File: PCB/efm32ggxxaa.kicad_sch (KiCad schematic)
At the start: 8 parts, among them U5 EFM32GG11B420F2048GQ100

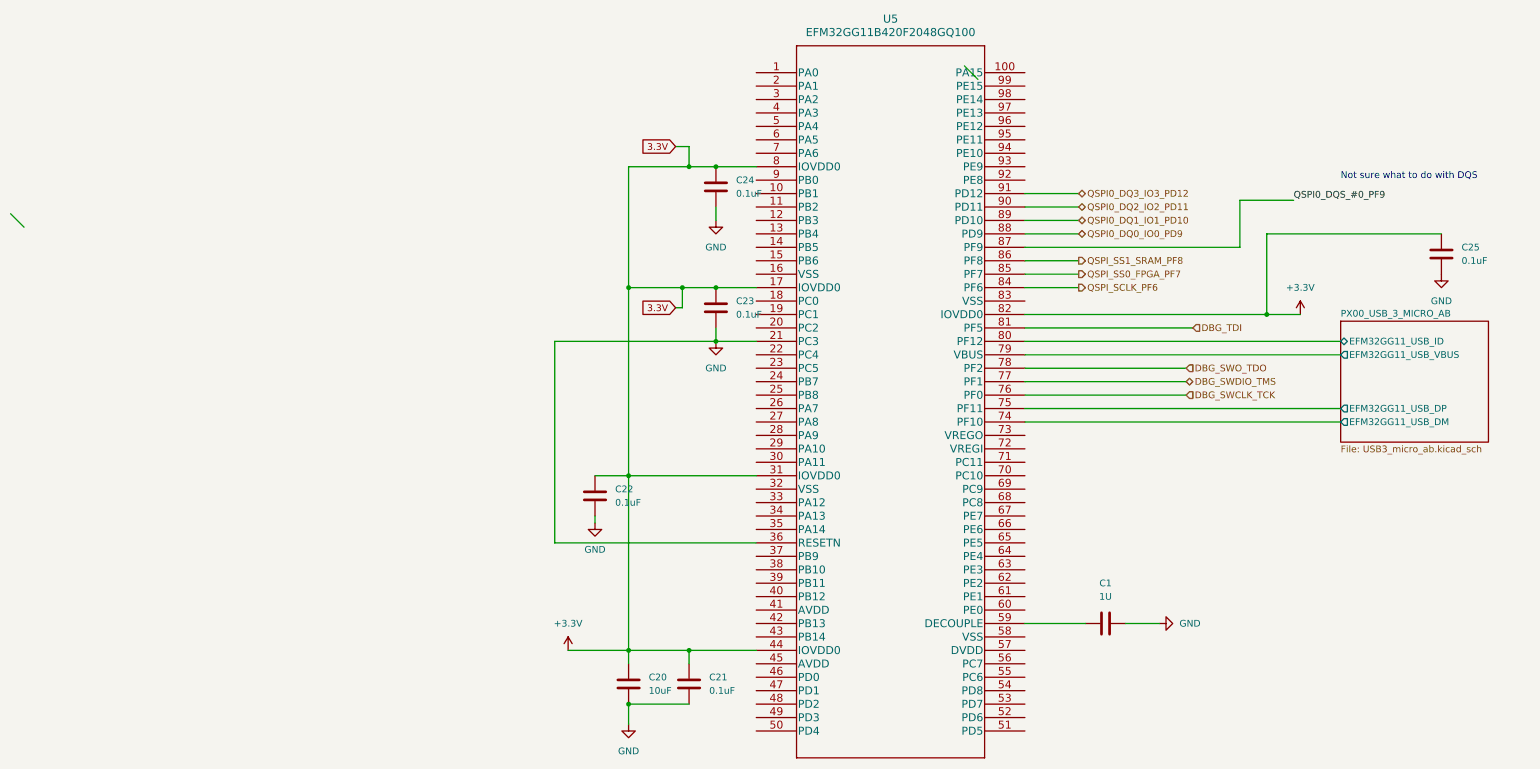
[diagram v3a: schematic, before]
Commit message: Attempt to set up SRAM
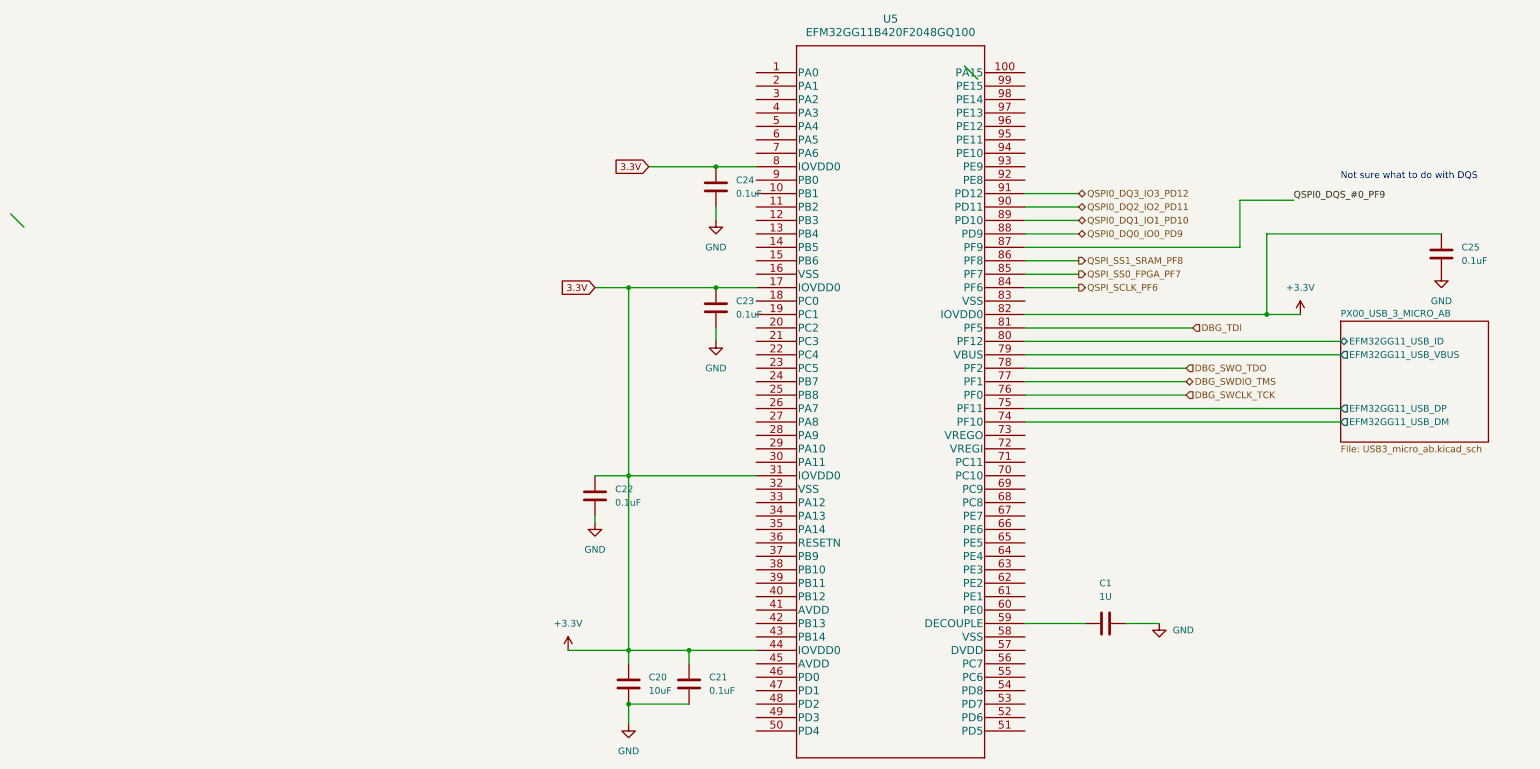
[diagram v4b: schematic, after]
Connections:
- net GND: no longer U5.21 (PC3), U5.36 (RESETN)
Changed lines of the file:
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@@
   (junction (at 99.06 107.95) (diameter 0) (color 0 0 0 0)
   )
-  (junction (at 109.22 72.39) (diameter 0) (color 0 0 0 0)
-  )
   (junction (at 115.57 49.53) (diameter 0) (color 0 0 0 0)
   )
@@
   (junction (at 99.06 140.97) (diameter 0) (color 0 0 0 0)
   )
-  (junction (at 110.49 49.53) (diameter 0) (color 0 0 0 0)
-  )
   (junction (at 219.71 77.47) (diameter 0) (color 0 0 0 0)
   )
-  (junction (at 115.57 82.55) (diameter 0) (color 0 0 0 0)
-  )
   (junction (at 115.57 72.39) (diameter 0) (color 0 0 0 0)
   )
@@
     (stroke (width 0) (type default))
   )
-  (wire (pts (xy 85.09 120.65) (xy 123.19 120.65))
-    (stroke (width 0) (type default))
-  )
   (wire (pts (xy 87.63 140.97) (xy 99.06 140.97))
     (stroke (width 0) (type default))
@@
     (stroke (width 0) (type default))
   )
-  (wire (pts (xy 99.06 49.53) (xy 99.06 72.39))
-    (stroke (width 0) (type default))
-  )
-  (wire (pts (xy 107.95 45.72) (xy 110.49 45.72))
-    (stroke (width 0) (type default))
-  )
   (wire (pts (xy 173.99 92.71) (xy 204.47 92.71))
     (stroke (width 0) (type default))
   )
-  (wire (pts (xy 110.49 49.53) (xy 115.57 49.53))
+  (wire (pts (xy 102.87 49.53) (xy 115.57 49.53))
     (stroke (width 0) (type default))
   )
@@
     (stroke (width 0) (type default))
   )
-  (wire (pts (xy 109.22 72.39) (xy 115.57 72.39))
-    (stroke (width 0) (type default))
-  )
   (wire (pts (xy 219.71 62.23) (xy 252.73 62.23))
     (stroke (width 0) (type default))
   )
-  (wire (pts (xy 115.57 82.55) (xy 123.19 82.55))
-    (stroke (width 0) (type default))
-  )
   (wire (pts (xy 99.06 140.97) (xy 110.49 140.97))
     (stroke (width 0) (type default))
@@
     (stroke (width 0) (type default))
   )
-  (wire (pts (xy 109.22 76.2) (xy 109.22 72.39))
-    (stroke (width 0) (type default))
-  )
-  (wire (pts (xy 85.09 82.55) (xy 85.09 120.65))
-    (stroke (width 0) (type default))
-  )
   (wire (pts (xy 115.57 49.53) (xy 123.19 49.53))
     (stroke (width 0) (type default))
@@
     (stroke (width 0) (type default))
   )
-  (wire (pts (xy 107.95 76.2) (xy 109.22 76.2))
+  (wire (pts (xy 92.71 72.39) (xy 99.06 72.39))
     (stroke (width 0) (type default))
   )
@@
     (stroke (width 0) (type default))
   )
-  (wire (pts (xy 99.06 49.53) (xy 110.49 49.53))
-    (stroke (width 0) (type default))
-  )
   (wire (pts (xy 173.99 87.63) (xy 204.47 87.63))
     (stroke (width 0) (type default))
@@
     (stroke (width 0) (type default))
   )
-  (wire (pts (xy 99.06 72.39) (xy 109.22 72.39))
+  (wire (pts (xy 99.06 72.39) (xy 115.57 72.39))
     (stroke (width 0) (type default))
   )
@@
     (stroke (width 0) (type default))
   )
-  (wire (pts (xy 110.49 45.72) (xy 110.49 49.53))
-    (stroke (width 0) (type default))
-  )
   (wire (pts (xy 173.99 62.23) (xy 184.15 62.23))
     (stroke (width 0) (type default))
@@
   )
   (wire (pts (xy 173.99 59.69) (xy 184.15 59.69))
-    (stroke (width 0) (type default))
-  )
-  (wire (pts (xy 85.09 82.55) (xy 115.57 82.55))
     (stroke (width 0) (type default))
   )
@@
     (effects (font (size 1.27 1.27)) (justify left bottom))
   )
-  (global_label "3.3V" (shape input) (at 107.95 45.72 180) (fields_autoplaced)
+  (global_label "3.3V" (shape input) (at 102.87 49.53 180) (fields_autoplaced)
     (effects (font (size 1.27 1.27)) (justify right))
-    (property "Intersheetrefs" "${INTERSHEET_REFS}" (at 100.8524 45.72 0)
+    (property "Intersheetrefs" "${INTERSHEET_REFS}" (at 95.7724 49.53 0)
       (effects (font (size 1.27 1.27)) (justify right) hide)
     )
   )
-  (global_label "3.3V" (shape input) (at 107.95 76.2 180) (fields_autoplaced)
+  (global_label "3.3V" (shape input) (at 92.71 72.39 180) (fields_autoplaced)
     (effects (font (size 1.27 1.27)) (justify right))
-    (property "Intersheetrefs" "${INTERSHEET_REFS}" (at 100.8524 76.2 0)
+    (property "Intersheetrefs" "${INTERSHEET_REFS}" (at 85.6124 72.39 0)
       (effects (font (size 1.27 1.27)) (justify right) hide)
     )
@@
     )
   )
-  (symbol (lib_id "power:GND") (at 199.39 135.89 90) (unit 1)
-    (in_bom yes) (on_board yes) (dnp no) (fields_autoplaced)
-    (property "Reference" "#PWR07" (at 205.74 135.89 0)
-      (effects (font (size 1.27 1.27)) hide)
-    )
-    (property "Value" "GND" (at 203.2 135.89 90)
-      (effects (font (size 1.27 1.27)) (justify right))
+  (symbol (lib_id "power:GND") (at 199.39 135.89 0) (unit 1)
+    (in_bom yes) (on_board yes) (dnp no) (fields_autoplaced)
+    (property "Reference" "#PWR07" (at 199.39 142.24 0)
+      (effects (font (size 1.27 1.27)) hide)
+    )
+    (property "Value" "GND" (at 201.93 137.16 0)
+      (effects (font (size 1.27 1.27)) (justify left))
     )
     (property "Footprint" "" (at 199.39 135.89 0)

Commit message: dump
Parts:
- added C65: 1U, symbol Device:C
- added J102: EFM32_PinHeader_PortE, Connector_PinHeader_2.54mm:PinHeader_2x06_P2.54mm_Vertical_SMD, symbol Connector_Generic:Conn_02x06_Odd_Even
- added Y101: 72MHz, Crystal:Crystal_SMD_2016-4Pin_2.0x1.6mm, symbol Device:Crystal_GND24
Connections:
- net GND: now also U5.58 (VSS), C65.2, Y101.2, Y101.4
- net at U5.42 (PB13): now also Y101.3
- net at U5.43 (PB14): now also Y101.1
- net PD0_UART1_TX: now reaches U5.46 (PD0)
- net PD0_UART1_TX: now also J102.10 (Pin_10)
- net PD1_UART1_RX: now reaches U5.47 (PD1)
- net PD1_UART1_RX: now also J102.12 (Pin_12)
- net PD2_MCU: now reaches U5.48 (PD2)
- net PD2_MCU: now also J102.8 (Pin_8)
- net PD3_UART1_CS: now reaches U5.49 (PD3)
- net PD3_UART1_CS: now also J102.9 (Pin_9)
- net PD4_UART1_RTS: now reaches U5.50 (PD4)
- net PD4_UART1_RTS: now also J102.11 (Pin_11)
- net PE0_MCU: now reaches U5.60 (PE0)
- net PE0_MCU: now also J102.1 (Pin_1)
- net PE5: now reaches U5.65 (PE5)
- net PE5: now also J102.7 (Pin_7)
- net at U5.73 (VREGO): now also C65.1
- new net PE1_MCU: J102.2 (Pin_2)
- new net PE2_MCU: J102.3 (Pin_3)
- new net PE3_MCU: J102.4 (Pin_4)
- new net PE4: J102.5 (Pin_5)
- new net PE6_MCU: J102.6 (Pin_6)
- no-connect marks 0 -> 1
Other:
- moved on the sheet: C20, C21

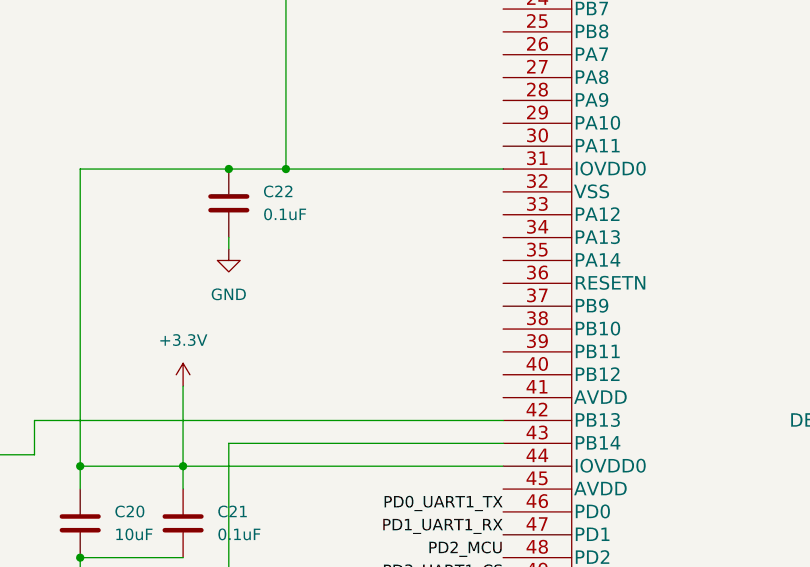
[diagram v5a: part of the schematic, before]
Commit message: add barrel jack
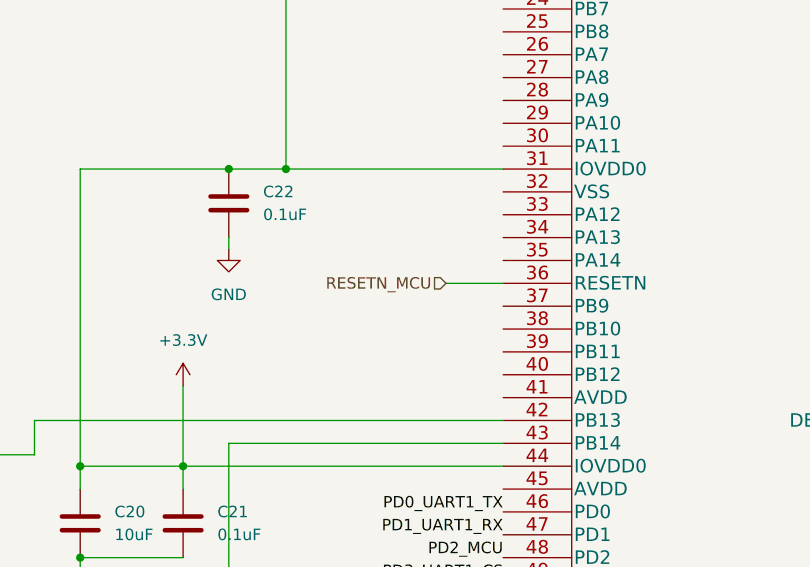
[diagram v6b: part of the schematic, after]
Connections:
- net RESETN_MCU: now reaches U5.36 (RESETN)
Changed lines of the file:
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@@
+    (stroke (width 0) (type default))
+  )
+  (wire (pts (xy 116.84 120.65) (xy 123.19 120.65))
     (stroke (width 0) (type default))
   )
@@
     (effects (font (size 1.27 1.27)) (justify left))
   )
+  (hierarchical_label "RESETN_MCU" (shape input) (at 116.84 120.65 180) (fields_autoplaced)
+    (effects (font (size 1.27 1.27)) (justify right))
+  )
   (hierarchical_label "QSPI0_DQ1_IO1_PD10" (shape bidirectional) (at 184.15 59.69 0) (fields_autoplaced)
